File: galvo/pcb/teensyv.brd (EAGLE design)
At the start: 101.6 x 44.1 mm, 46 parts, among them IC1 RB-0512D, IC10 MCP4922-E/P, IC2.5 MAX6102, IC3 QUAD_OPAMPP, IC5 MAX6105, IC9 QUAD_OPAMPP

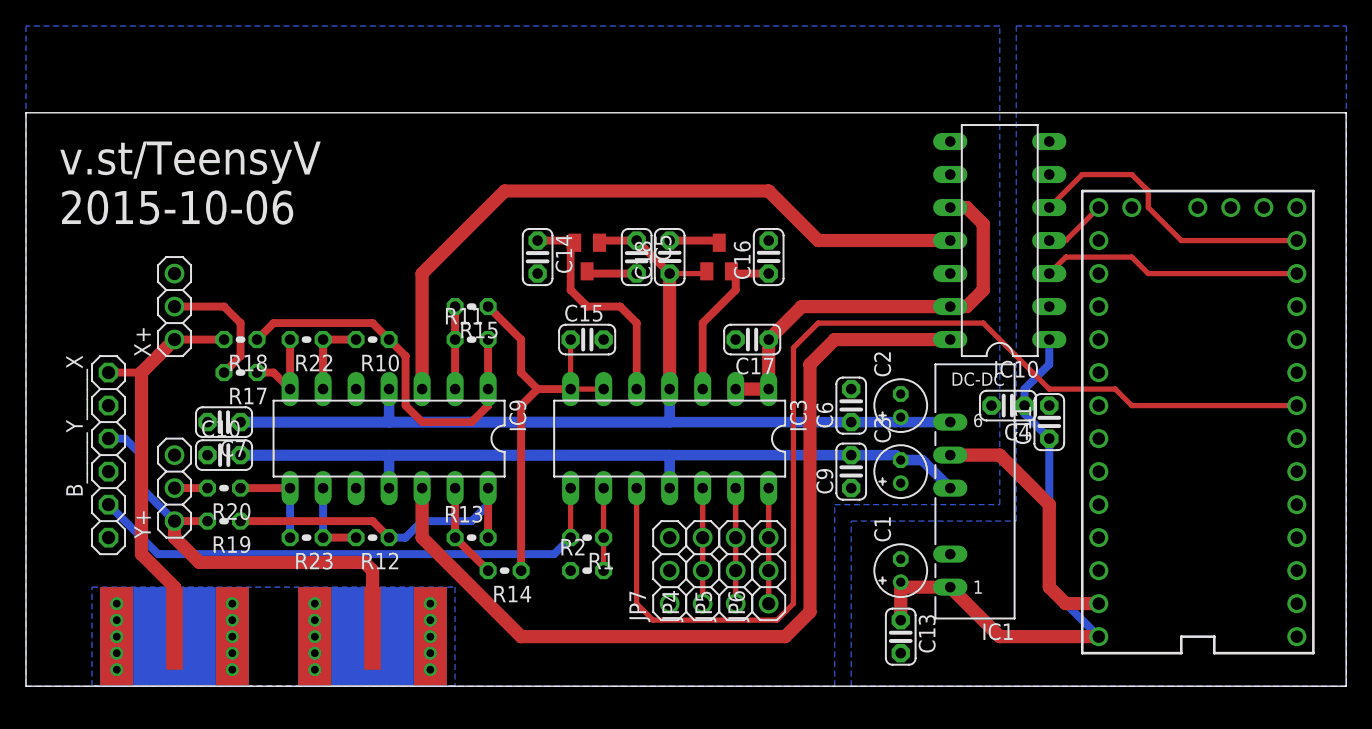
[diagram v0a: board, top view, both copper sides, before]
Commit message: added LEDs and extra header
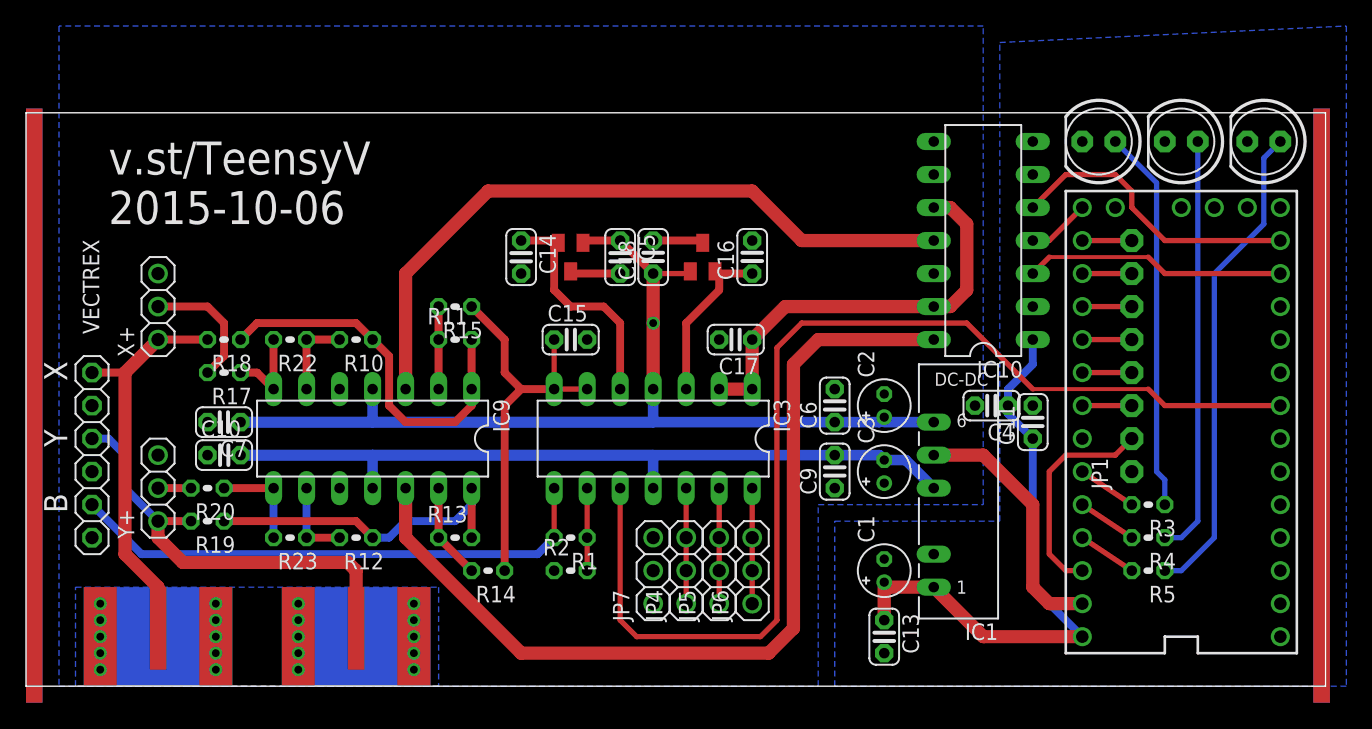
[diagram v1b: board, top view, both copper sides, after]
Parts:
- removed B_____Y_____X: (no value), adafruit:1X06
- added JP1: (no value), adafruit:1X08-CLEANBIG
- added LED1, LED2, LED3: (no value), adafruit:LED5MM
- added R3, R4, R5: 10k, adafruit:0204V
- added VECTREX: (no value), adafruit:1X06
- moved IC1 1.27 mm to (69.8, 14.0)
- moved IC10 1.27 mm to (73.7, 34.3)
- moved C15 1.27 mm to (41.9, 26.7)
- moved C17 1.27 mm to (54.6, 26.7)
- moved C18 1.27 mm to (48.3, 33.0)
- moved C5 1.27 mm to (45.7, 33.0)
- moved C6 1.27 mm to (62.2, 21.6)
- moved C9 1.27 mm to (62.2, 16.5)
- moved IC2.5 1.27 mm to (41.9, 33.0)
- moved IC3 1.27 mm to (48.3, 19.1)
- moved IC5 1.27 mm to (52.1, 33.0)
- moved JP4 1.27 mm to (50.8, 8.89)
- moved JP7 1.27 mm to (48.3, 8.89)
- moved R1 1.27 mm to (41.9, 11.4)
- moved R10 1.27 mm to (25.4, 26.7)
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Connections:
- net !SS2 renamed A6
- removed net 3.3V: U$1.3.3V, U$1.3.3V1
- new net +3V: JP1.2, U$1.3.3V, U$1.3.3V1
- new net A0: JP1.8, U$1.14/A0
- new net A1: JP1.7, U$1.15/A1
- new net A2: JP1.6, U$1.16/A2
- new net A3: JP1.5, U$1.17/A3
- new net A4: JP1.4, U$1.18/A4
- new net A5: JP1.3, U$1.19/A5
- new net LED1: R3.2, U$1.21/A7
- new net LED2: R4.2, U$1.22/A8
- new net LED3: R5.2, U$1.23/A9
- new net N$11: LED2.A, R4.1
- new net N$12: LED3.A, R5.1
- new net N$7: LED1.A, R3.1
- net AGND: now also VECTREX.2, VECTREX.4, VECTREX.6; no longer B_____Y_____X.2, B_____Y_____X.4, B_____Y_____X.6
- net BRIGHT: now also VECTREX.5; no longer B_____Y_____X.5
- net GND: now also JP1.1, LED1.K, LED2.K, LED3.K
- net X+: now also VECTREX.1; no longer B_____Y_____X.1
- net Y+: now also VECTREX.3; no longer B_____Y_____X.3
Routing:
- net N$12: track 0.00 -> 37.4 mm
- net N$11: track 0.00 -> 32.3 mm
- net N$7: track 0.00 -> 29.5 mm
- net +3V: track 0.00 -> 16.8 mm
- net LED3: track 0.00 -> 4.58 mm
- net LED2: track 0.00 -> 4.58 mm
- net LED1: track 0.00 -> 4.58 mm
- net A5: track 0.00 -> 3.81 mm
- net A4: track 0.00 -> 3.81 mm
- net A3: track 0.00 -> 3.81 mm
- net A2: track 0.00 -> 3.81 mm
- net A1: track 0.00 -> 3.81 mm
- net A0: track 0.00 -> 3.81 mm
- net +12V: track 111.6 -> 109.1 mm, vias 0 -> 1
- net -12V: track 93.8 -> 91.2 mm
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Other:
- board size 101.6 x 44.1 mm -> 100 x 44.1 mm
- board text added: "B"
- board text added: "X"
- board text added: "Y"

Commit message: reworked board to have two DACs and proper differential amplifier
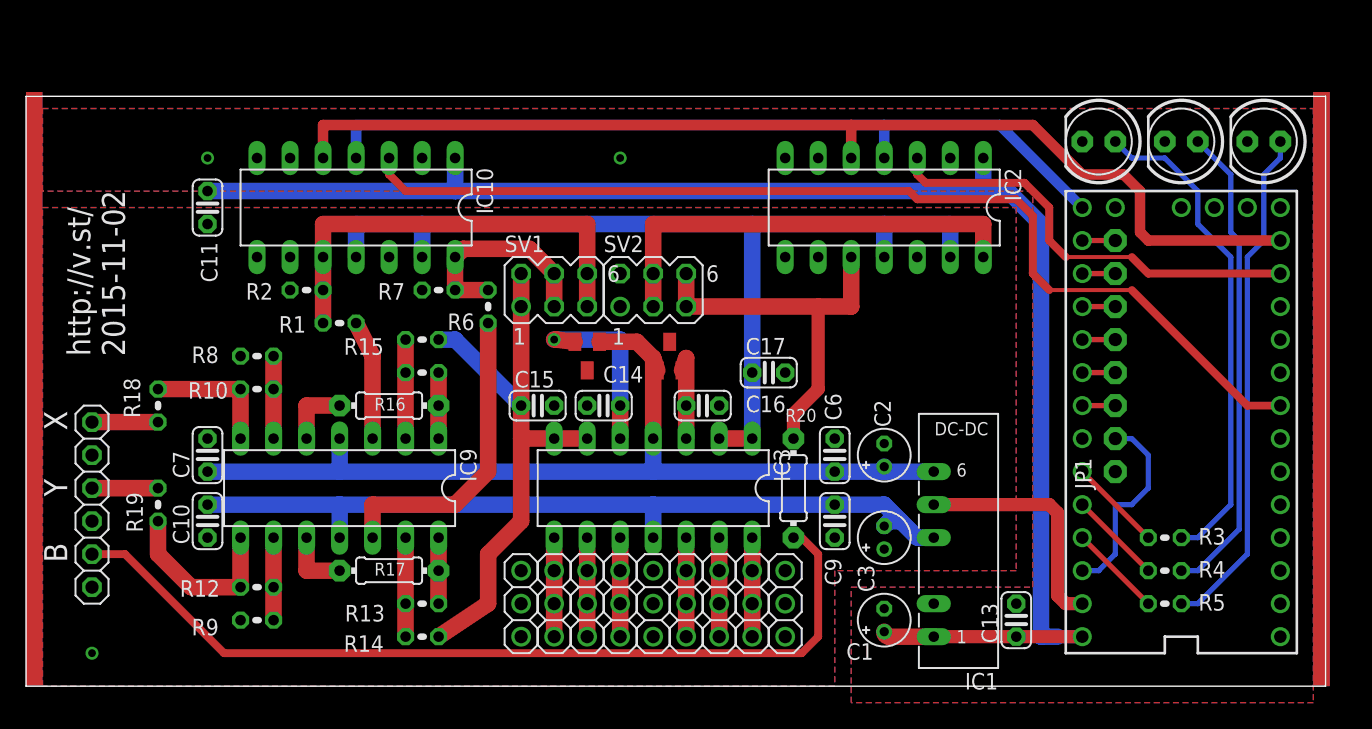
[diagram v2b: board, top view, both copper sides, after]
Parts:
- removed C18, C4, C5: 0.1uF, adafruit:C025-024X044
- removed R22, R23: 10k, adafruit:0204V
- removed U$2, U$9: BNC, adafruit:BNC-EDGE
- removed X+, Y+: (no value), adafruit:1X03
- added IC2: MCP4922-E/P, nh-ic:DIL14
- added JP10, JP2, JP3, JP8, JP9: (no value), adafruit:1X03
- added R16: (no value), adafruit:0204/7
- added R6, R7, R8, R9: 10k, adafruit:0204V
- added SV1, SV2: (no value), con-lstb:MA03-2
- R17, R20: value 75r -> (none); device adafruit:0204V -> adafruit:0204/7
- R3, R4, R5: value 10k -> 400R
- moved C11 65.6 mm to (14.0, 36.8), turned to 270 degrees
- moved IC10 48.3 mm to (25.4, 36.8), turned to 180 degrees
- moved R20 45.1 mm to (59.1, 15.2), turned to 270 degrees
- moved R2 29.6 mm to (21.6, 30.5)
- moved R1 24.3 mm to (24.1, 27.9), turned to 0 degrees
- moved R17 19.8 mm to (27.9, 8.89)
- moved C14 13.1 mm to (44.5, 21.6), turned to 180 degrees
- moved C16 12.0 mm to (52.1, 21.6), turned to 0 degrees
- moved JP7 10.5 mm to (58.4, 6.35)
- moved C13 10.2 mm to (76.2, 5.08), turned to 90 degrees
- moved R10 8.52 mm to (17.8, 22.9), turned to 0 degrees
- moved R12 8.52 mm to (17.8, 7.62), turned to 0 degrees
- moved IC5 8.03 mm to (49.5, 25.4)
- moved IC2.5 7.73 mm to (43.2, 25.4)
- moved R14 7.18 mm to (30.5, 3.81)
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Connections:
- removed net BRIGHT: IC3.8, R1.2, VECTREX.5
- removed net X-: R17.2, X+.2
- removed net Y-: R20.2, Y+.2
- new net DACW: IC2.14, SV2.3, SV2.4
- new net DACZ: IC2.10, R20.1, SV2.5, SV2.6
- new net N$14: IC9.8, R12.1, R19.1
- new net N$16: IC9.9, R12.2, R9.1
- new net N$17: IC9.6, R10.2, R8.1
- new net N$20: IC3.8, JP8.1, JP8.2, JP8.3
- new net N$21: IC9.5, R16.2
- new net N$22: IC9.10, R17.2
- new net N$23: R20.2, VECTREX.5
- net !SS0: now also IC2.3; no longer IC10.3
- net !SS1: now also IC10.3; no longer IC3.10
- net +12V: no longer C18.1, C5.1
- net +5V: now also IC2.1; no longer C4.1
- net AGND: now also C11.2, IC2.12, IC2.8, JP10.1, JP10.2, JP10.3, R7.1, R8.2, R9.2, SV2.1, SV2.2; no longer C18.2, C4.2, C5.2, IC10.9, IC9.10, IC9.5, U$2.SHELL$1, U$2.SHELL$2, U$2.SHELL$3, U$9.SHELL$1, U$9.SHELL$2, U$9.SHELL$3, X+.3, Y+.3
- net DACX: now also IC10.10, R1.1, R2.2, SV1.5, SV1.6; no longer IC10.11, IC9.3
- net DACY: now also R6.1, R7.2, SV1.3, SV1.4; no longer IC9.12
- net DIN: now also IC2.5
- net GND: no longer C11.2
- net N$13: now also R10.1, R18.1; no longer R17.1, R22.2
- net N$15: now also R17.1; no longer R12.1, R19.1
- net N$18: now also IC3.9, JP3.1, JP3.2, JP3.3; no longer IC9.8, R20.1, R23.2
- net N$19: now also IC3.10, JP2.1, JP2.2, JP2.3; no longer IC9.9, R12.2, R23.1
- net N$2: now also IC9.3, R1.2; no longer IC3.9, R1.1, R2.2
- net N$8: now also R16.1; no longer R10.1, R18.1
- net N$9: now also IC9.12, R6.2; no longer IC9.6, R10.2, R22.1
- net SCK: now also IC2.4
- net VREF2.5: now also SV1.1, SV1.2
- net VREF5: now also IC10.11, IC2.11, IC2.13; no longer IC10.10
- net X+: no longer U$9.IN, X+.1
- net Y+: no longer U$2.IN, Y+.1
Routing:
- net +5V: track 45.9 -> 120.6 mm
- net N$23: track 0.00 -> 68.3 mm
- net DIN: track 23.0 -> 84.3 mm
- net SCK: track 4.86 -> 63.6 mm
- net DACY: track 70.0 -> 16.3 mm
- net VREF5: track 32.6 -> 74.9 mm
- net BRIGHT: track 41.5 -> 0.00 mm
- net +12V: track 109.1 -> 73.2 mm, vias 1 -> 0
- net DACW: track 0.00 -> 34.3 mm
- net DACZ: track 0.00 -> 30.0 mm
- net Y+: track 33.7 -> 5.08 mm
- net -12V: track 91.2 -> 63.4 mm
- net X+: track 30.7 -> 5.08 mm
- net N$8: track 29.3 -> 5.08 mm
- net N$15: track 25.7 -> 5.08 mm
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- added copper zone on layer 1, net AGND
- added copper zone on layer 1, net GND
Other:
- board size 100 x 44.1 mm -> 100 x 45.4 mm
- board text added: "http://v.st/ 2015-11-02"
- board text removed: "v.st/TeensyV 2015-10-06"

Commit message: ground plane tweaks
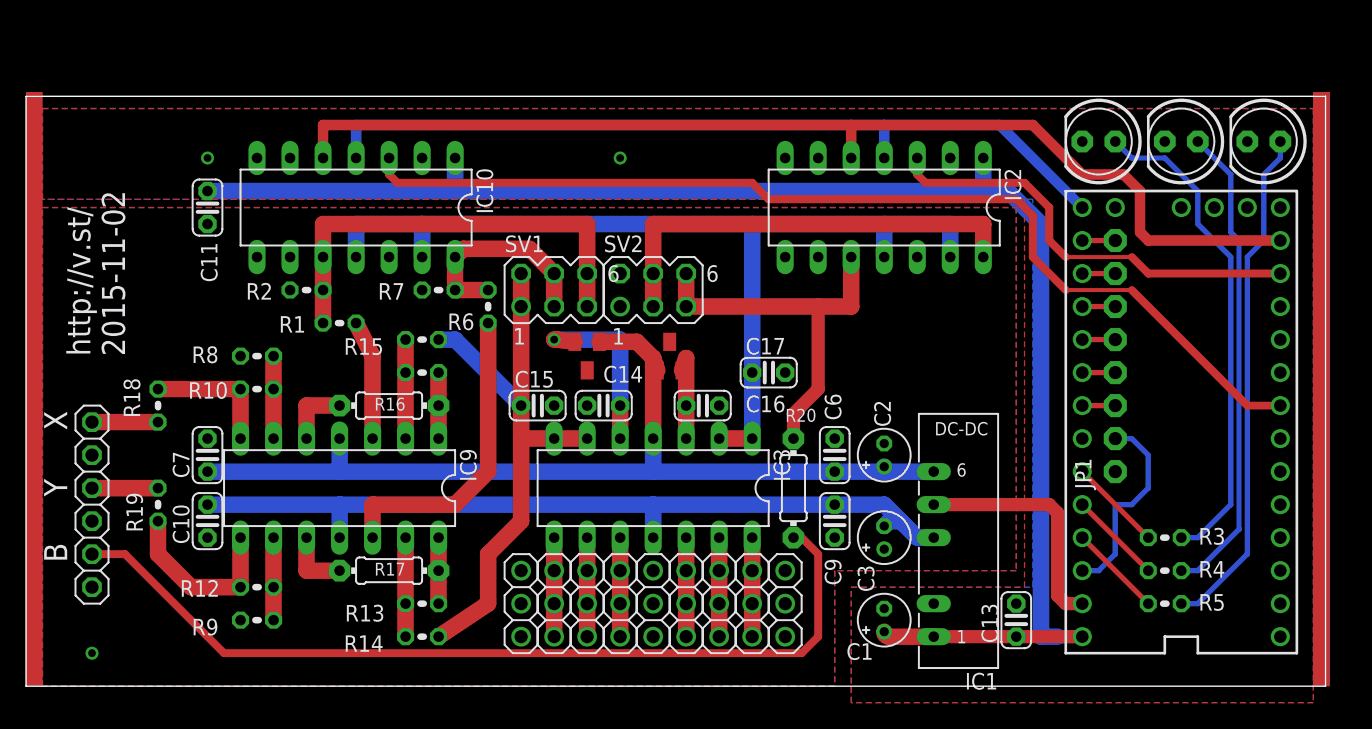
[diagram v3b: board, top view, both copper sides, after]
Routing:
- net !SS1: track 79.8 -> 79.1 mm
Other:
- board text added: "+3"
- board text added: "A0"
- board text added: "A1"
- board text added: "A2"
- board text added: "A3"
- board text added: "A4"
- board text added: "A5"
- board text added: "GND"
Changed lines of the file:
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@@
 <text x="3.175" y="14.605" size="1.778" layer="25" font="vector" rot="R90">Y</text>
 <text x="3.175" y="19.685" size="1.778" layer="25" font="vector" rot="R90">X</text>
+<text x="87.63" y="18.415" size="1.27" layer="26" font="vector" rot="MR0">+3</text>
+<text x="87.63" y="20.955" size="1.27" layer="26" font="vector" rot="MR0">A0</text>
+<text x="87.63" y="23.495" size="1.27" layer="26" font="vector" rot="MR0">A1</text>
+<text x="87.63" y="26.035" size="1.27" layer="26" font="vector" rot="MR0">A2</text>
+<text x="87.63" y="28.575" size="1.27" layer="26" font="vector" rot="MR0">A3</text>
+<text x="87.63" y="31.115" size="1.27" layer="26" font="vector" rot="MR0">A4</text>
+<text x="87.63" y="33.655" size="1.27" layer="26" font="vector" rot="MR0">A5</text>
+<text x="88.9" y="15.875" size="1.27" layer="26" font="vector" rot="MR0">GND</text>
 </plain>
 <attributes>
@@
 <vertex x="63.5" y="7.62"/>
 <vertex x="77.47" y="7.62"/>
-<vertex x="77.47" y="38.1"/>
-<vertex x="1.27" y="38.1"/>
+<vertex x="77.47" y="37.465"/>
+<vertex x="1.27" y="37.465"/>
 </polygon>
 <contactref element="C13" pad="2"/>
@@
 <vertex x="63.5" y="-1.27"/>
 <vertex x="63.5" y="7.62"/>
-<vertex x="77.47" y="7.62"/>
-<vertex x="77.47" y="38.1"/>
-<vertex x="1.27" y="38.1"/>
+<vertex x="76.835" y="7.62"/>
+<vertex x="76.835" y="37.465"/>
+<vertex x="1.27" y="37.465"/>
 </polygon>
 <via x="13.97" y="40.64" extent="1-16" drill="0.6" shape="square"/>
@@
 <wire x1="96.52" y1="21.59" x2="93.98" y2="21.59" width="0.6096" layer="1"/>
 <wire x1="93.98" y1="21.59" x2="85.09" y2="30.48" width="0.6096" layer="1"/>
-<wire x1="85.09" y1="30.48" x2="78.74" y2="30.48" width="0.3048" layer="1"/>
-<wire x1="78.74" y1="30.48" x2="77.47" y2="31.75" width="0.6096" layer="1"/>
-<wire x1="77.47" y1="31.75" x2="77.47" y2="36.195" width="0.6096" layer="1"/>
+<wire x1="85.09" y1="30.48" x2="80.01" y2="30.48" width="0.3048" layer="1"/>
+<wire x1="80.01" y1="30.48" x2="77.47" y2="33.02" width="0.6096" layer="1"/>
+<wire x1="77.47" y1="33.02" x2="77.47" y2="36.195" width="0.6096" layer="1"/>
 <wire x1="77.47" y1="36.195" x2="76.2" y2="37.465" width="0.6096" layer="1"/>
-<wire x1="76.2" y1="37.465" x2="68.58" y2="37.465" width="0.6096" layer="1"/>
-<wire x1="68.58" y1="37.465" x2="67.945" y2="38.1" width="0.6096" layer="1"/>
-<wire x1="67.945" y1="38.1" x2="29.21" y2="38.1" width="0.6096" layer="1"/>
-<wire x1="29.21" y1="38.1" x2="27.94" y2="39.37" width="0.6096" layer="1"/>
+<wire x1="76.2" y1="37.465" x2="57.15" y2="37.465" width="0.6096" layer="1"/>
+<wire x1="57.15" y1="37.465" x2="55.88" y2="38.735" width="0.6096" layer="1"/>
+<wire x1="55.88" y1="38.735" x2="28.575" y2="38.735" width="0.6096" layer="1"/>
+<wire x1="28.575" y1="38.735" x2="27.94" y2="39.37" width="0.6096" layer="1"/>
 <wire x1="27.94" y1="39.37" x2="27.94" y2="40.64" width="0.6096" layer="1"/>
 </signal>
@@
 </signal>
 </signals>
+<errors>
+</errors>
 </board>
 </drawing>

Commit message: convert to inverting opamp
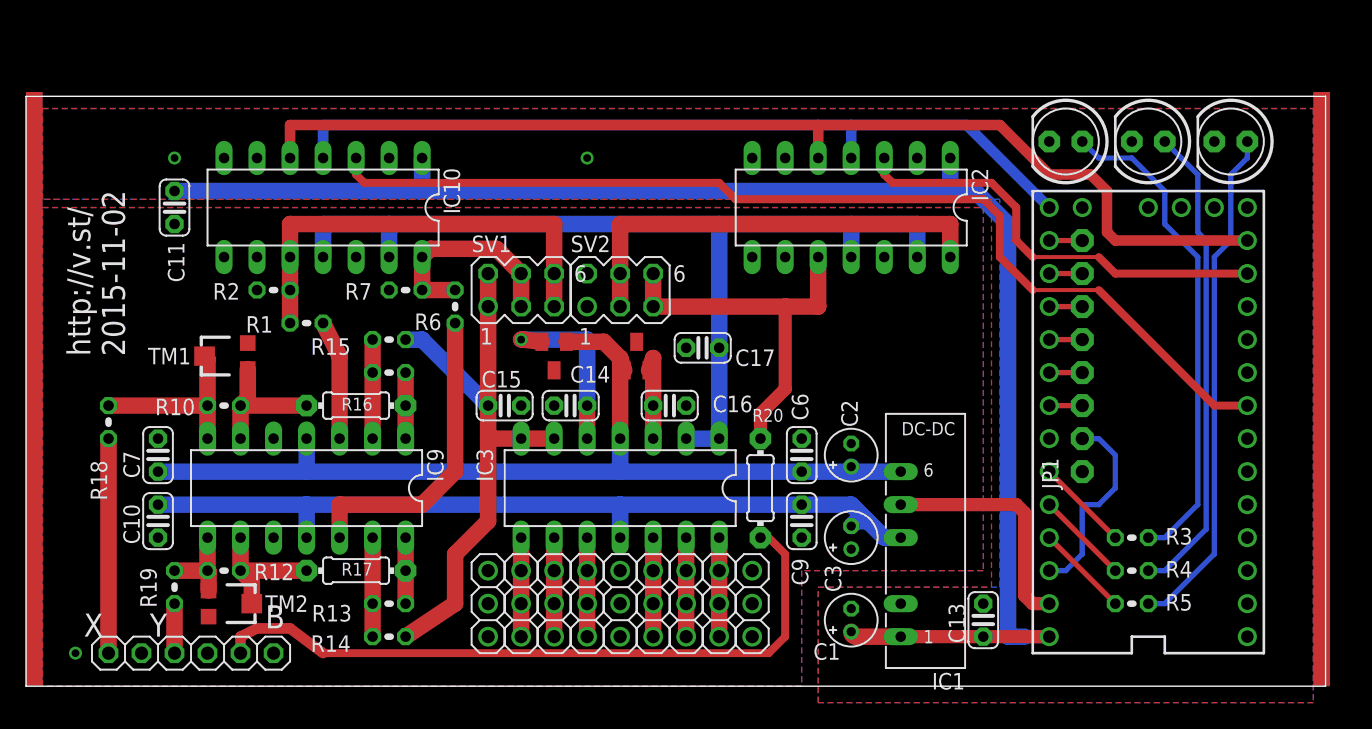
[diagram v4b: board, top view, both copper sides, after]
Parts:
- removed R8, R9: 10k, adafruit:0204V
- added TM1, TM2: (no value), adafruit:TC33X
- moved VECTREX 13.7 mm to (12.7, 2.54), turned to 0 degrees
- moved R19 6.48 mm to (11.4, 7.62), turned to 270 degrees
- moved C17 5.43 mm to (52.1, 26.0), turned to 180 degrees
- moved R18 4.02 mm to (6.35, 20.3)
- moved C10 3.81 mm to (10.2, 12.7)
- moved C7 3.81 mm to (10.2, 17.8)
- moved R12 2.84 mm to (15.2, 8.89)
- moved R10 2.84 mm to (15.2, 21.6)
- moved C1 2.54 mm to (63.5, 5.08)
- moved C13 2.54 mm to (73.7, 5.08)
- moved C14 2.54 mm to (41.9, 21.6)
- moved C2 2.54 mm to (63.5, 17.8)
- moved C3 2.54 mm to (63.5, 11.4)
- moved IC2 2.54 mm to (63.5, 36.8)
- moved JP5 2.54 mm to (50.8, 6.35)
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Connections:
- removed net N$21: IC9.5, R16.2
- removed net N$22: IC9.10, R17.2
- net AGND: now also IC9.10, IC9.5; no longer R8.2, R9.2
- net N$13: now also TM1.2
- net N$14: now also TM2.1
- net N$16: now also R17.2, TM2.2; no longer R9.1
- net N$17: now also R16.2, TM1.1; no longer R8.1
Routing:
- net N$23: track 68.3 -> 53.3 mm
- net X+: track 5.08 -> 16.5 mm
- net N$14: track 13.8 -> 6.65 mm
- net N$22: track 5.08 -> 0.00 mm
- net N$21: track 5.08 -> 0.00 mm
- net N$17: track 6.35 -> 10.7 mm
- net N$16: track 6.35 -> 10.5 mm
- net N$13: track 10.2 -> 14.1 mm
- net -12V: track 63.4 -> 64.7 mm
- net +12V: track 73.2 -> 74.5 mm
- net Y+: track 5.08 -> 3.81 mm
